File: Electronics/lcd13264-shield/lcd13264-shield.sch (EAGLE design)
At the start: 28 parts, among them J1 MICRO-SDCARD-CONNECTOR-330006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, J2 ARDUINO_R3_SHIELDUNO_R3_SHIEL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, Q1 PNP-500mA, X1 FH12-12S-1S, X2 FH12-12S-1S

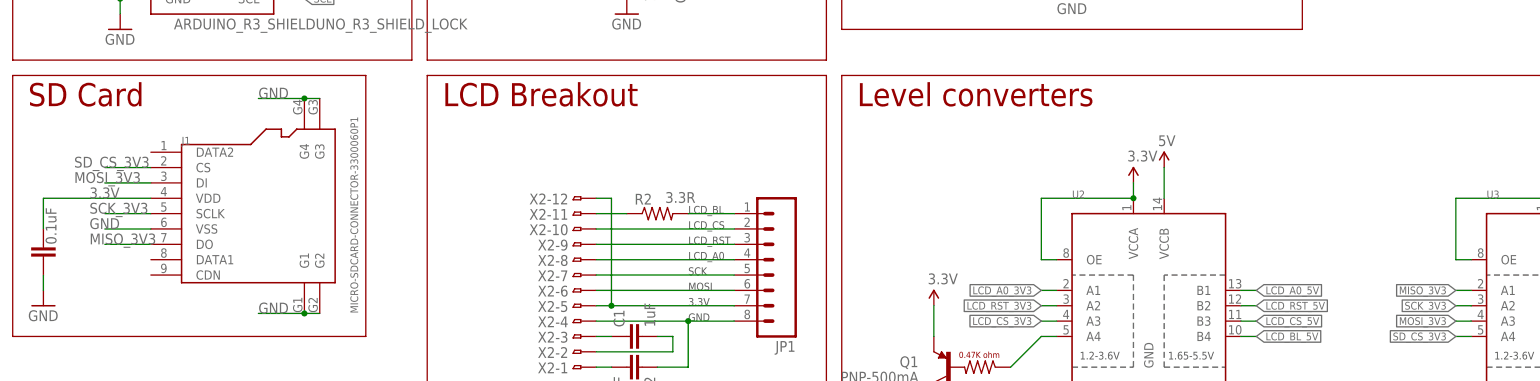
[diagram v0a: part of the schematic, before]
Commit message: Added bypass caps to level shifter. This closes #1.
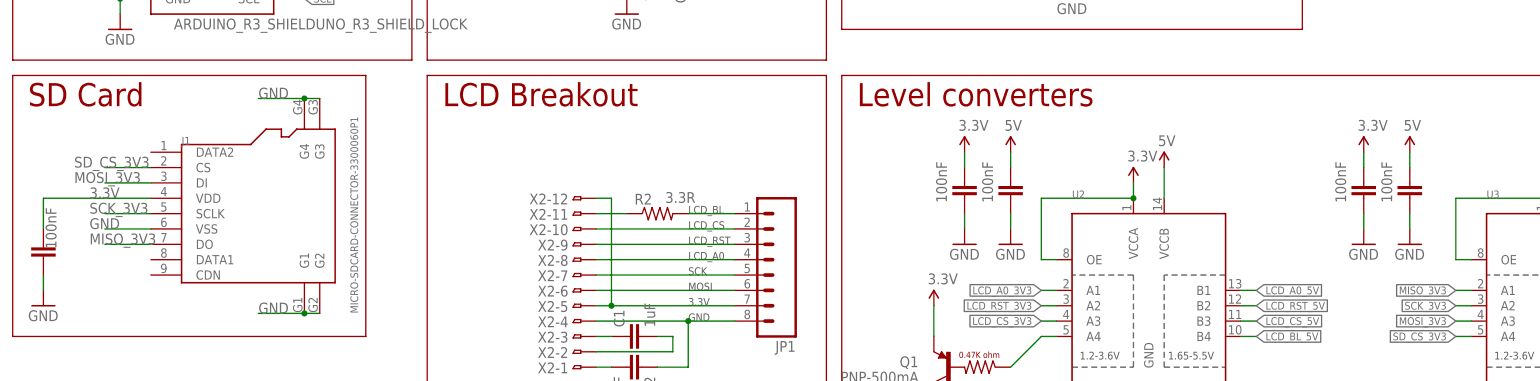
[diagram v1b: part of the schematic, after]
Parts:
- added C3, C4, C5, C6: 100nF, PaxInstrument-T400:SPARKFUN-CAPACITORS_CAP0603-CAP
- C21: value 0.1uF -> 100nF
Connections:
- net 3.3V: now also C3.2, C5.2
- net 5V: now also C4.2, C6.2
- net GND: now also C3.1, C4.1, C5.1, C6.1
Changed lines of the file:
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@@
 <part name="J1" library="PaxInstrument-T400" deviceset="MICRO-SDCARD-CONNECTOR" device="-3300060P1"/>
 <part name="X1" library="PaxInstrument-T400" deviceset="FH12-12S-1S" device=""/>
-<part name="C21" library="PaxInstrument-T400" deviceset="SPARKFUN-CAPACITORS_CAP" device="0603-CAP" value="0.1uF">
+<part name="C21" library="PaxInstrument-T400" deviceset="SPARKFUN-CAPACITORS_CAP" device="0603-CAP" value="100nF">
 <attribute name="MPN" value="CL10B104KO8NNNC"/>
 <attribute name="OC_DIGIKEY" value="1276-1005-2-ND"/>
@@
 <part name="P+5" library="SparkFun" deviceset="3.3V" device=""/>
 <part name="J2" library="SparkFun-Boards" deviceset="ARDUINO_R3_SHIELD" device="UNO_R3_SHIELD_LOCK"/>
+<part name="C3" library="PaxInstrument-T400" deviceset="SPARKFUN-CAPACITORS_CAP" device="0603-CAP" value="100nF">
+<attribute name="MPN" value="CL10B104KO8NNNC"/>
+<attribute name="OC_DIGIKEY" value="1276-1005-2-ND"/>
+</part>
+<part name="C4" library="PaxInstrument-T400" deviceset="SPARKFUN-CAPACITORS_CAP" device="0603-CAP" value="100nF">
+<attribute name="MPN" value="CL10B104KO8NNNC"/>
+<attribute name="OC_DIGIKEY" value="1276-1005-2-ND"/>
+</part>
+<part name="P+6" library="SparkFun" deviceset="3.3V" device=""/>
+<part name="SUPPLY4" library="SparkFun-Aesthetics" deviceset="5V" device=""/>
+<part name="GND4" library="SparkFun-Aesthetics" deviceset="GND" device=""/>
+<part name="GND5" library="SparkFun-Aesthetics" deviceset="GND" device=""/>
+<part name="C5" library="PaxInstrument-T400" deviceset="SPARKFUN-CAPACITORS_CAP" device="0603-CAP" value="100nF">
+<attribute name="MPN" value="CL10B104KO8NNNC"/>
+<attribute name="OC_DIGIKEY" value="1276-1005-2-ND"/>
+</part>
+<part name="C6" library="PaxInstrument-T400" deviceset="SPARKFUN-CAPACITORS_CAP" device="0603-CAP" value="100nF">
+<attribute name="MPN" value="CL10B104KO8NNNC"/>
+<attribute name="OC_DIGIKEY" value="1276-1005-2-ND"/>
+</part>
+<part name="P+7" library="SparkFun" deviceset="3.3V" device=""/>
+<part name="SUPPLY5" library="SparkFun-Aesthetics" deviceset="5V" device=""/>
+<part name="GND7" library="SparkFun-Aesthetics" deviceset="GND" device=""/>
+<part name="GND8" library="SparkFun-Aesthetics" deviceset="GND" device=""/>
 </parts>
 <sheets>
@@
 <instance part="P+5" gate="G$1" x="160.02" y="149.86"/>
 <instance part="J2" gate="G$1" x="40.64" y="223.52"/>
+<instance part="C3" gate="G$1" x="165.1" y="170.18" smashed="yes" rot="R180">
+<attribute name="OC_DIGIKEY" x="165.1" y="170.18" size="1.778" layer="96" rot="R180" display="off"/>
+<attribute name="VALUE" x="160.401" y="173.736" size="1.778" layer="96" rot="R270"/>
+<attribute name="MPN" x="165.1" y="170.18" size="1.778" layer="96" rot="R180" display="off"/>
+</instance>
+<instance part="C4" gate="G$1" x="172.72" y="170.18" smashed="yes" rot="R180">
+<attribute name="OC_DIGIKEY" x="172.72" y="170.18" size="1.778" layer="96" rot="R180" display="off"/>
+<attribute name="VALUE" x="168.021" y="173.736" size="1.778" layer="96" rot="R270"/>
+<attribute name="MPN" x="172.72" y="170.18" size="1.778" layer="96" rot="R180" display="off"/>
+</instance>
+<instance part="P+6" gate="G$1" x="165.1" y="175.26"/>
+<instance part="SUPPLY4" gate="G$1" x="172.72" y="175.26"/>
+<instance part="GND4" gate="1" x="165.1" y="160.02"/>
+<instance part="GND5" gate="1" x="172.72" y="160.02"/>
+<instance part="C5" gate="G$1" x="231.14" y="170.18" smashed="yes" rot="R180">
+<attribute name="OC_DIGIKEY" x="231.14" y="170.18" size="1.778" layer="96" rot="R180" display="off"/>
+<attribute name="VALUE" x="226.441" y="173.736" size="1.778" layer="96" rot="R270"/>
+<attribute name="MPN" x="231.14" y="170.18" size="1.778" layer="96" rot="R180" display="off"/>
+</instance>
+<instance part="C6" gate="G$1" x="238.76" y="170.18" smashed="yes" rot="R180">
+<attribute name="OC_DIGIKEY" x="238.76" y="170.18" size="1.778" layer="96" rot="R180" display="off"/>
+<attribute name="VALUE" x="234.061" y="173.736" size="1.778" layer="96" rot="R270"/>
+<attribute name="MPN" x="238.76" y="170.18" size="1.778" layer="96" rot="R180" display="off"/>
+</instance>
+<instance part="P+7" gate="G$1" x="231.14" y="175.26"/>
+<instance part="SUPPLY5" gate="G$1" x="238.76" y="175.26"/>
+<instance part="GND7" gate="1" x="231.14" y="160.02"/>
+<instance part="GND8" gate="1" x="238.76" y="160.02"/>
 </instances>
 <busses>
@@
 <pinref part="P+5" gate="G$1" pin="3.3V"/>
 </segment>
+<segment>
+<pinref part="P+6" gate="G$1" pin="3.3V"/>
+<pinref part="C3" gate="G$1" pin="2"/>
+<wire x1="165.1" y1="175.26" x2="165.1" y2="172.72" width="0.1524" layer="91"/>
+</segment>
+<segment>
+<pinref part="P+7" gate="G$1" pin="3.3V"/>
+<pinref part="C5" gate="G$1" pin="2"/>
+<wire x1="231.14" y1="175.26" x2="231.14" y2="172.72" width="0.1524" layer="91"/>
+</segment>
 </net>
 <net name="GND" class="0">
@@
 <wire x1="264.16" y1="132.08" x2="264.16" y2="134.62" width="0.1524" layer="91"/>
 </segment>
+<segment>
+<pinref part="GND4" gate="1" pin="GND"/>
+<pinref part="C3" gate="G$1" pin="1"/>
+<wire x1="165.1" y1="162.56" x2="165.1" y2="165.1" width="0.1524" layer="91"/>
+</segment>
+<segment>
+<pinref part="C4" gate="G$1" pin="1"/>
+<pinref part="GND5" gate="1" pin="GND"/>
+<wire x1="172.72" y1="165.1" x2="172.72" y2="162.56" width="0.1524" layer="91"/>
+</segment>
+<segment>
+<pinref part="GND7" gate="1" pin="GND"/>
+<pinref part="C5" gate="G$1" pin="1"/>
+<wire x1="231.14" y1="162.56" x2="231.14" y2="165.1" width="0.1524" layer="91"/>
+</segment>
+<segment>
+<pinref part="C6" gate="G$1" pin="1"/>
+<pinref part="GND8" gate="1" pin="GND"/>
+<wire x1="238.76" y1="165.1" x2="238.76" y2="162.56" width="0.1524" layer="91"/>
+</segment>
 </net>
 <net name="MISO_3V3" class="0">
@@
 <wire x1="266.7" y1="172.72" x2="266.7" y2="167.64" width="0.1524" layer="91"/>
 </segment>
-</net>
+<segment>
+<pinref part="SUPPLY4" gate="G$1" pin="5V"/>
+<pinref part="C4" gate="G$1" pin="2"/>
+<wire x1="172.72" y1="175.26" x2="172.72" y2="172.72" width="0.1524" layer="91"/>
+</segment>
+<segment>
+<pinref part="SUPPLY5" gate="G$1" pin="5V"/>
+<pinref part="C6" gate="G$1" pin="2"/>
+<wire x1="238.76" y1="175.26" x2="238.76" y2="172.72" width="0.1524" layer="91"/>
+</segment>
+</net>

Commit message: Aupdated shield. Not sure what.
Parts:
- added SJ1, SJ2: JUMPER-PAD-2-NC_BY_PASTE, SparkFun-Passives:JUMPER-PAD-2-NC_BY_PASTE
- added SJ3: JUMPER-PTH-2-NC, SparkFun-Passives:JUMPER-PTH-2-NC
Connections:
- net N$16 renamed D3
- net N$36 renamed AREF
- removed net N$45: C2.1, JP1.8, X2-4.1
- net GND: now also C2.1, JP1.8, X2-4.1
- net SCL: now also SJ2.1, SJ2.2
- net SDA: now also SJ1.1, SJ1.2

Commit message: Close to done. Need to review.
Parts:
- removed J2: ARDUINO_R3_SHIELDUNO_R3_SHIELD_LOCK, SparkFun-Boards:ARDUINO_R3_SHIELDUNO_R3_SHIELD_LOCK
- added J3: ARDUINO_R3_SHIELDUNO_R3_SHIELD_NOLABELS_LOCK, SparkFun-Boards:ARDUINO_R3_SHIELDUNO_R3_SHIELD_NOLABELS_LOCK
- added SJ10, SJ11, SJ12, SJ13, SJ14, SJ19, SJ20, SJ21, SJ22, SJ23, SJ24, SJ25, SJ26, SJ4, SJ5, SJ6, SJ7, SJ8, SJ9: JUMPER-PAD-2-NC_BY_PASTE, SparkFun-Passives:JUMPER-PAD-2-NC_BY_PASTE
- C1, C2, C21, C3, C35, C36, C4, C5, C6: device PaxInstrument-T400:SPARKFUN-CAPACITORS_CAP0603-CAP -> PaxInstrument-T400:SPARKFUN-CAPACITORS_CAP1206
- R1, R11, R12, R15, R16, R19, R2, R8: device PaxInstrument-T400:SPARKFUN-RESISTORS_RESISTOR0603-RES -> PaxInstrument-T400:SPARKFUN-RESISTORS_RESISTOR1206
- SJ3: value JUMPER-PTH-2-NC -> JUMPER-PAD-2-NC_BY_PASTE; device SparkFun-Passives:JUMPER-PTH-2-NC -> SparkFun-Passives:JUMPER-PAD-2-NC_BY_PASTE
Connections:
- removed net LCD_A0_5V: J2.*D9, U2.B1
- removed net LCD_BL_5V: J2.*D6, U2.B4
- removed net LCD_CS_5V: J2.D7, U2.B3
- removed net LCD_RST_5V: J2.D8, U2.B2
- removed net MISO_5V: J2.D12, U3.B1
- removed net MOSI_5V: J2.*D11, U3.B3
- removed net N$1: J2.IOREF
- removed net N$17: J2.D2
- removed net N$20: J2.TX
- removed net N$25: J2.RX
- removed net N$31: J2.A4
- removed net N$33: J2.A5
- removed net N$34: J2.RES
- removed net N$35: J2.VIN
- removed net SCK_5V: J2.D13, U3.B2
- removed net SD_CS_5V: J2.*D10, U3.B4
- removed net SW_A: J2.D4, R8.2, S3.2
- removed net SW_B: J2.*D5, R11.2, S2.2
- removed net SW_C: J2.A3, R12.2, S1.2
- removed net SW_D: J2.A2, R15.2, S4.2
- removed net SW_E: J2.A1, R16.2, S5.2
- removed net SW_F: J2.A0, R1.2, S6.2
- new net A0: J3.A0, R1.2, S6.2, SJ10.1, SJ10.2
- new net A1: J3.A1, R16.2, S5.2, SJ7.1, SJ7.2
- new net A2: J3.A2, R15.2, S4.2, SJ11.1, SJ11.2
- new net A3: J3.A3, R12.2, S1.2, SJ12.1, SJ12.2
- new net A4: J3.A4, SJ13.1, SJ13.2
- new net A5: J3.A5, SJ14.1, SJ14.2
- new net D0: J3.RX, SJ8.1, SJ8.2
- new net D1: J3.TX, SJ9.1, SJ9.2
- new net D10: J3.*D10, SJ23.1, SJ23.2, U3.B1
- new net D11(MOSI): J3.*D11, SJ24.1, SJ24.2, U3.B3
- new net D12(MISO): J3.D12, SJ25.1, SJ25.2, U3.B2
- new net D13(SCK): J3.D13, SJ26.1, SJ26.2, U3.B4
- new net D2: J3.D2, SJ3.1, SJ3.2
- new net D4: J3.D4, R8.2, S3.2, SJ5.1, SJ5.2
- new net D5: J3.*D5, R11.2, S2.2, SJ6.1, SJ6.2
- new net D6: J3.*D6, SJ19.1, SJ19.2, U2.B4
- new net D7: J3.D7, SJ20.1, SJ20.2, U2.B3
- new net D8: J3.D8, SJ21.1, SJ21.2, U2.B2
- new net D9: J3.*D9, SJ22.1, SJ22.2, U2.B1
- new net IOREF: J3.IOREF
- new net RESET: J3.RES
- new net VIN: J3.VIN
- net 3.3V: now also J3.3.3V; no longer J2.3.3V
- net 5V: now also J3.5V; no longer J2.5V
- net AREF: now also J3.AREF; no longer J2.AREF
- net D3: now also J3.*D3, SJ4.1, SJ4.2; no longer J2.*D3
- net GND: now also J3.GND@0, J3.GND@1, J3.GND@2; no longer J2.GND@0, J2.GND@1, J2.GND@2
- net MISO_3V3: now also U3.A2; no longer U3.A1
- net SCK_3V3: now also U3.A4; no longer U3.A2
- net SCL: now also J3.SCL; no longer J2.SCL
- net SDA: now also J3.SDA; no longer J2.SDA
- net SD_CS_3V3: now also U3.A1; no longer U3.A4
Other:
- note added: "Jumpers"
- moved on the sheet: J1, Q1, U2

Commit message: Changed all passives to 0805 and updated traces. Passes DRC.
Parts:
- C21, C3, C35, C36, C4, C5, C6: device PaxInstrument-T400:SPARKFUN-CAPACITORS_CAP1206 -> PaxInstrument-T400:SPARKFUN-CAPACITORS_CAP0603-CAP
- R1, R11, R12, R15, R16, R19, R2, R8: device PaxInstrument-T400:SPARKFUN-RESISTORS_RESISTOR1206 -> PaxInstrument-T400:SPARKFUN-RESISTORS_RESISTOR0603-RES

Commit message: Closed all the silkscreen issues.
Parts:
- C1, C2: device PaxInstrument-T400:SPARKFUN-CAPACITORS_CAP1206 -> PaxInstrument-T400:SPARKFUN-CAPACITORS_CAP0603-CAP
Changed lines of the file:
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@@
 <part name="SUPPLY1" library="SparkFun-Aesthetics" deviceset="5V" device=""/>
 <part name="R2" library="PaxInstrument-T400" deviceset="SPARKFUN-RESISTORS_RESISTOR" device="0603-RES" value="3.3R"/>
-<part name="C1" library="PaxInstrument-T400" deviceset="SPARKFUN-CAPACITORS_CAP" device="1206" value="1uF">
+<part name="C1" library="PaxInstrument-T400" deviceset="SPARKFUN-CAPACITORS_CAP" device="0603-CAP" value="1uF">
 <attribute name="MPN" value="LMK107B7105KA-T"/>
 <attribute name="OC_DIGIKEY" value="587-1242-2-ND"/>
 </part>
-<part name="C2" library="PaxInstrument-T400" deviceset="SPARKFUN-CAPACITORS_CAP" device="1206" value="1uF">
+<part name="C2" library="PaxInstrument-T400" deviceset="SPARKFUN-CAPACITORS_CAP" device="0603-CAP" value="1uF">
 <attribute name="MPN" value="LMK107B7105KA-T"/>
 <attribute name="OC_DIGIKEY" value="587-1242-2-ND"/>
